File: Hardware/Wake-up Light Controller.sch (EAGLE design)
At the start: 46 parts, among them IC1 ST1S10, IC2 HT7333, IC3 DS3231/SO, IC4 ATMEGA328P_TQFP, J1 AVR-ISP, J2 Debug, Q1 BSS138, Q2 BSS138, Q3 FDN306P, Q4 IRLZ44N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

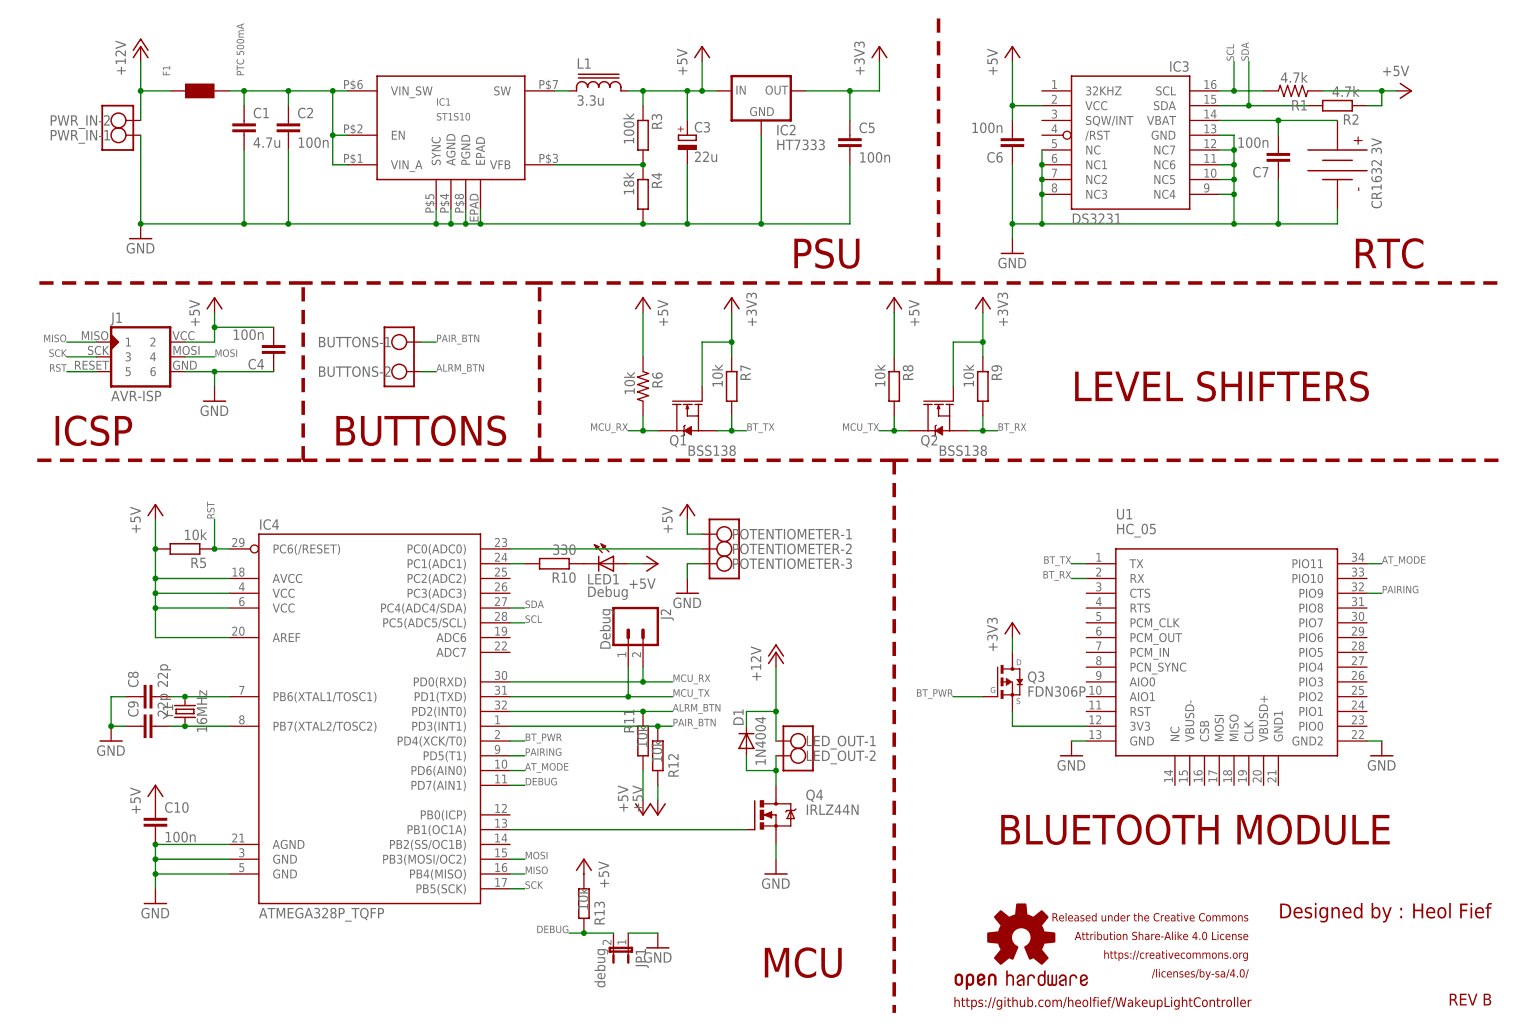
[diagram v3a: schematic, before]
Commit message: Add overvoltage protection
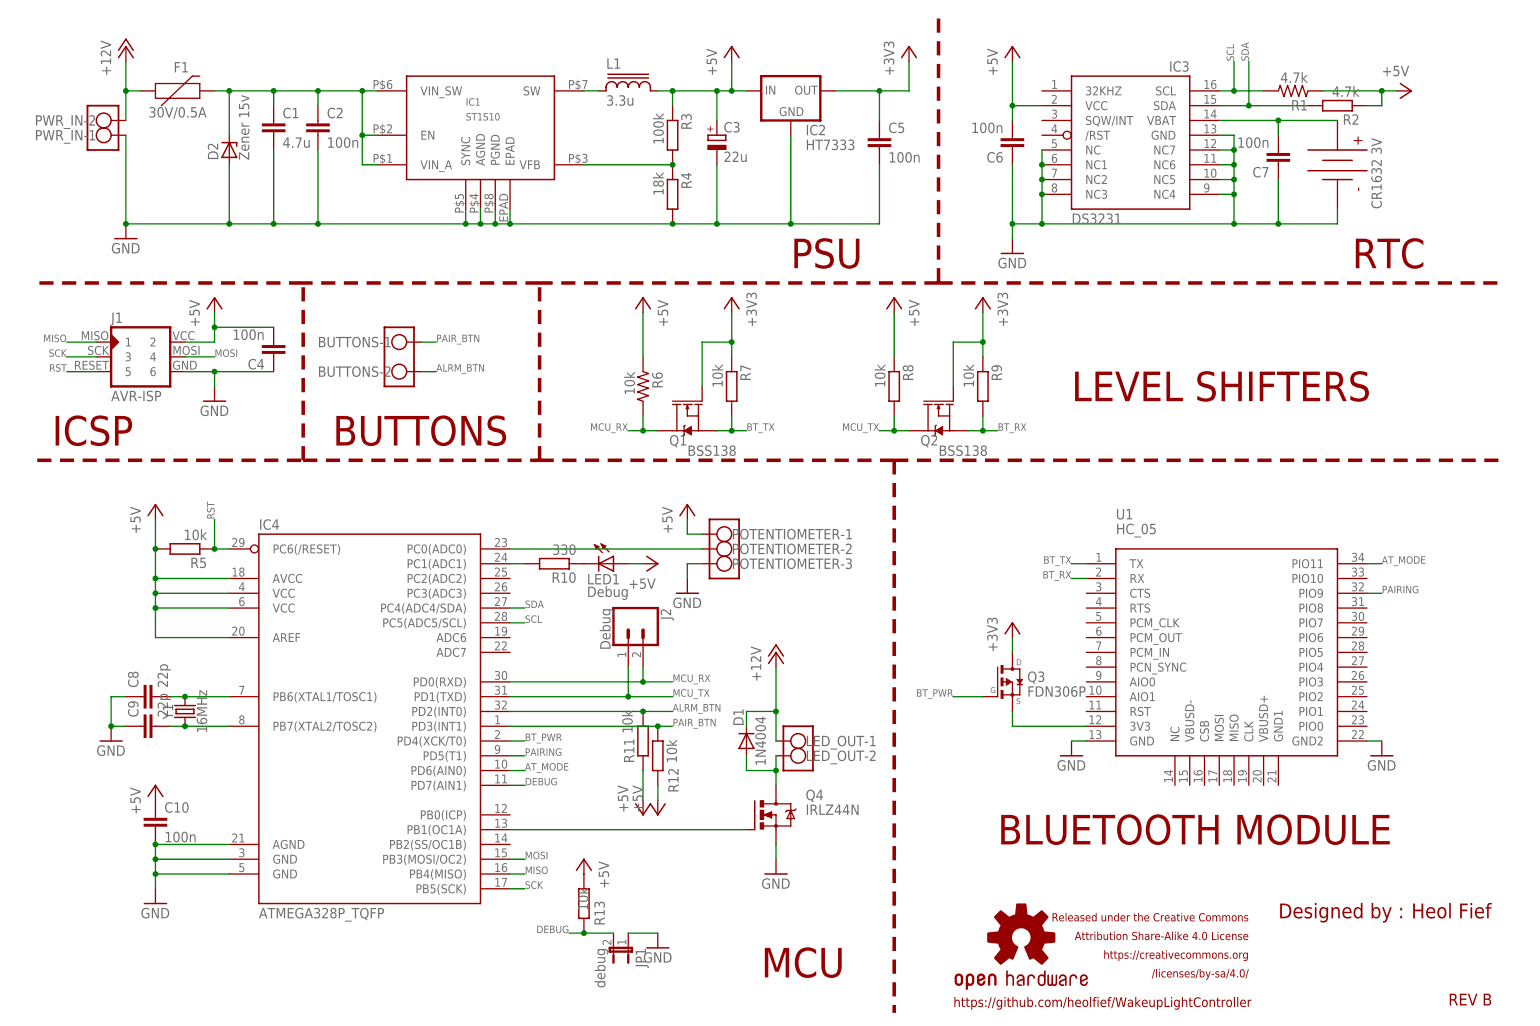
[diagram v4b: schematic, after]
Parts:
- added D2: Zener 15v, diode:ZENER-DIODESOD80C
- F1: value PTC 500mA -> 30V/0.5A; device BaseApp:PTC-0.2A-IH/0.5A-IT/40A-IM -> SparkFun-Fuses:PPTC_PTH
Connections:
- net GND: now also D2.A
- net N$9: now also D2.C
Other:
- moved on the sheet: C1, C2, C3, C5, IC1, IC2, L1, PWR_IN-1, PWR_IN-2, R3, R4

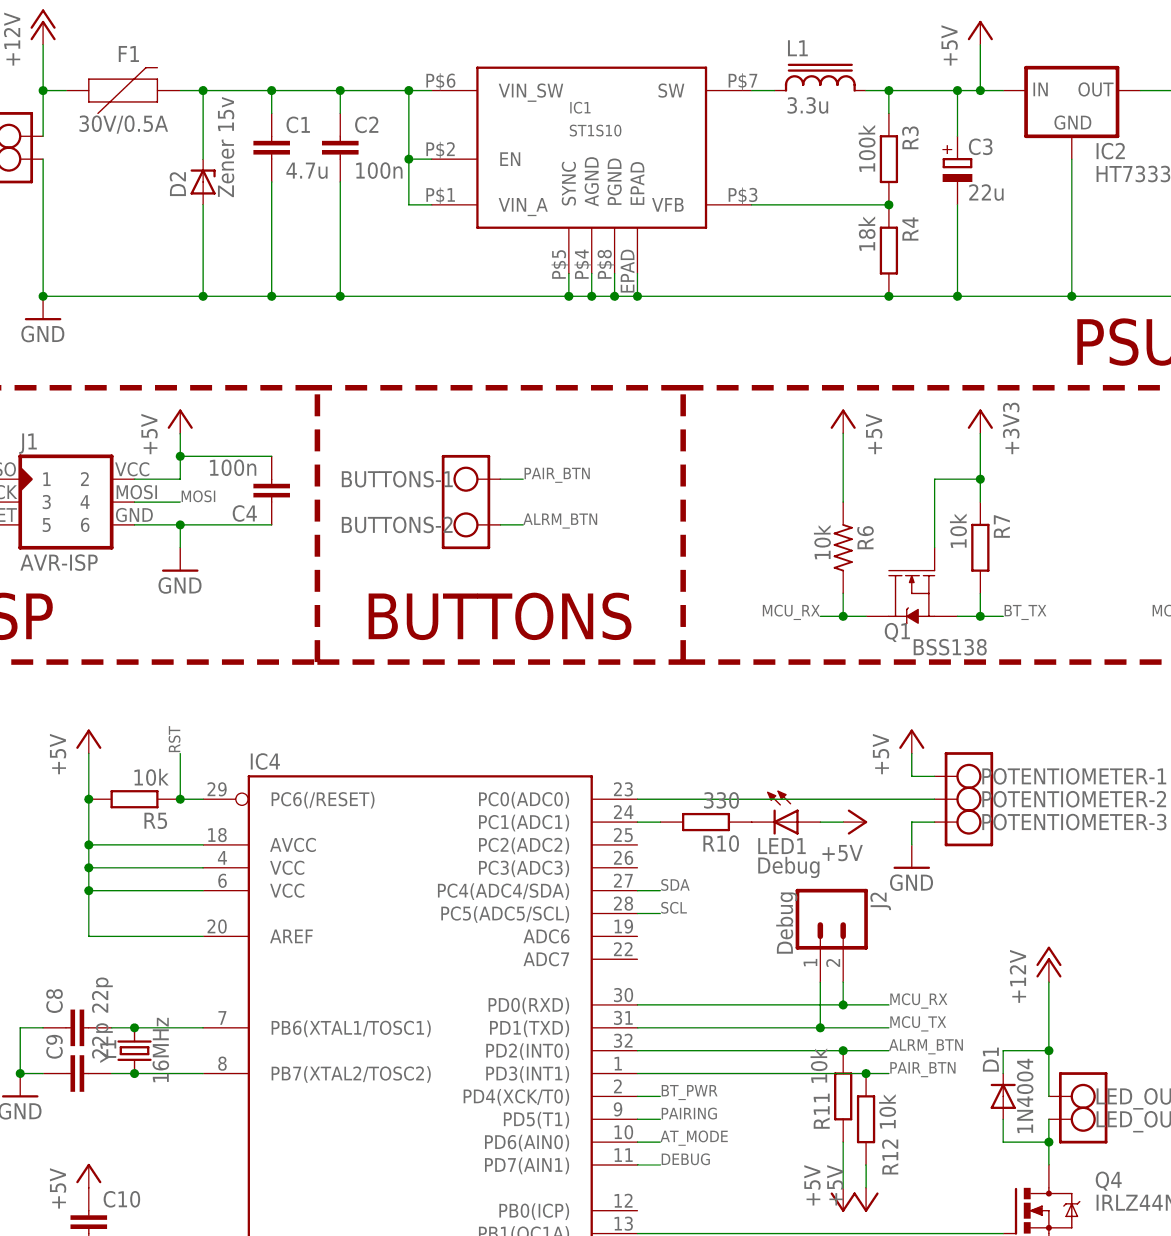
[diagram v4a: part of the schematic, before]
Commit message: Change diodes names
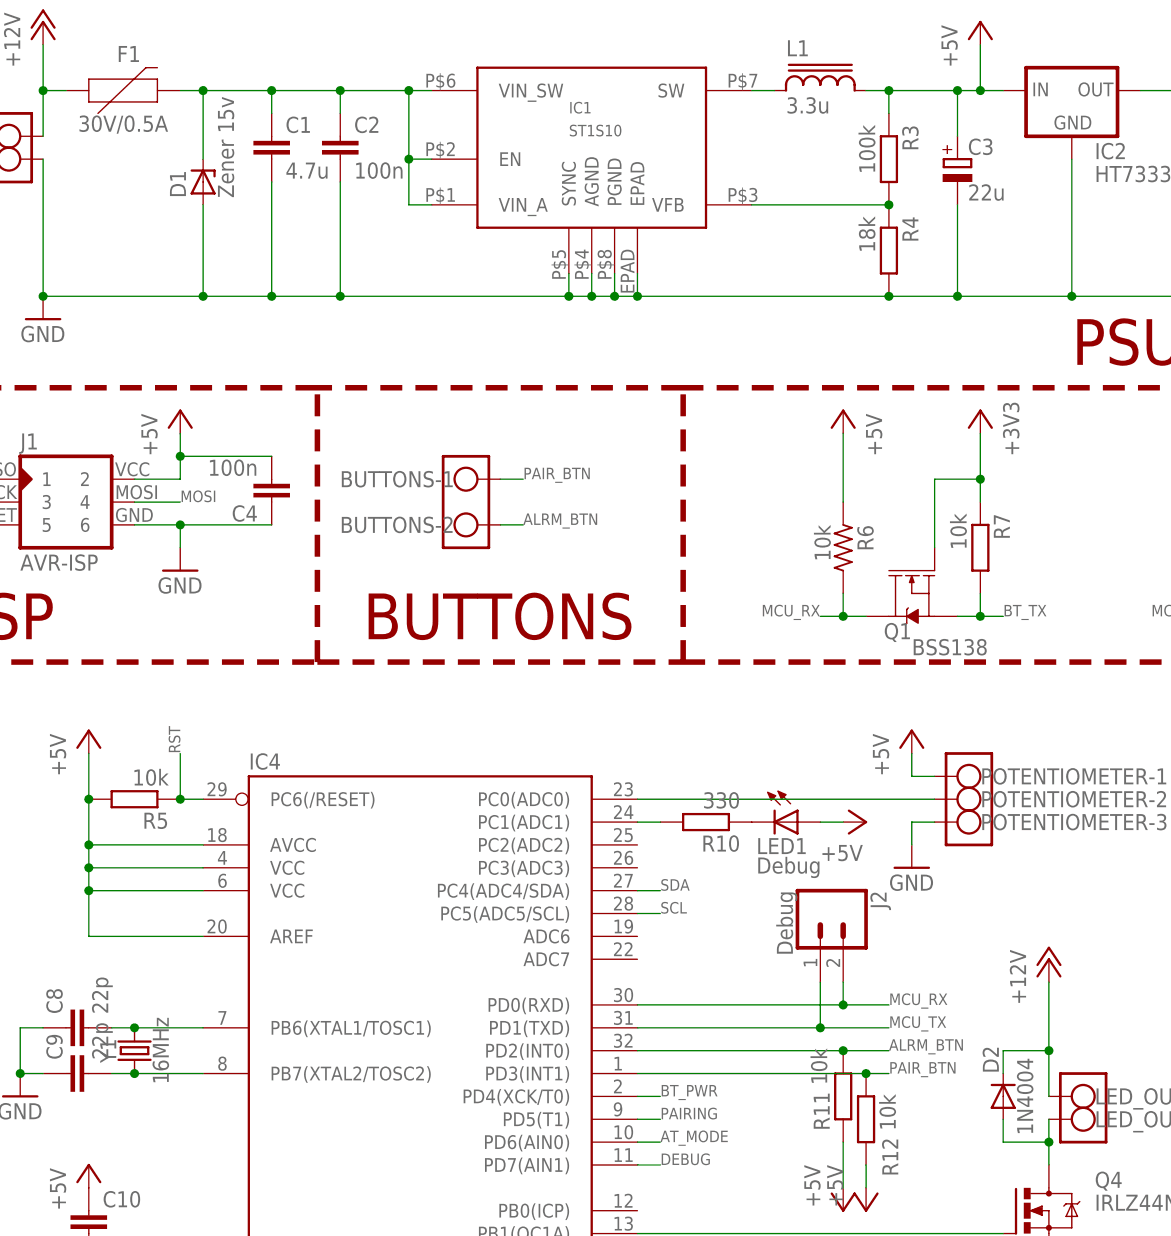
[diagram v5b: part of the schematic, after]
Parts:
- D1: value 1N4004 -> Zener 15v; device diode:DIODE-DO-214AC -> diode:ZENER-DIODESOD80C
- D2: value Zener 15v -> 1N4004; device diode:ZENER-DIODESOD80C -> diode:DIODE-DO-214AC
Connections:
- net +12V: now also D2.C; no longer D1.C
- net GND: now also D1.A; no longer D2.A
- net N$1: now also D2.A; no longer D1.A
- net N$9: now also D1.C; no longer D2.C
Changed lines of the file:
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@@
 <part name="P+8" library="supply1" deviceset="+12V" device=""/>
 <part name="GND8" library="supply1" deviceset="GND" device=""/>
-<part name="D1" library="diode" library_urn="urn:adsk.eagle:library:210" deviceset="DIODE-" device="DO-214AC" package3d_urn="urn:adsk.eagle:package:43416/2" value="1N4004"/>
+<part name="D2" library="diode" library_urn="urn:adsk.eagle:library:210" deviceset="DIODE-" device="DO-214AC" package3d_urn="urn:adsk.eagle:package:43416/2" value="1N4004"/>
 <part name="R5" library="resistor" library_urn="urn:adsk.eagle:library:348" deviceset="R-EU_" device="M0805" package3d_urn="urn:adsk.eagle:package:26079/1" value="10k"/>
 <part name="GND2" library="supply1" deviceset="GND" device=""/>
@@
 <part name="P+15" library="supply1" library_urn="urn:adsk.eagle:library:371" deviceset="+5V" device=""/>
 <part name="F1" library="SparkFun-Fuses" library_urn="urn:adsk.eagle:library:517" deviceset="PPTC" device="_PTH" package3d_urn="urn:adsk.eagle:package:38574/1" value="30V/0.5A"/>
-<part name="D2" library="diode" library_urn="urn:adsk.eagle:library:210" deviceset="ZENER-DIODE" device="SOD80C" package3d_urn="urn:adsk.eagle:package:43405/2" value="Zener 15v"/>
+<part name="D1" library="diode" library_urn="urn:adsk.eagle:library:210" deviceset="ZENER-DIODE" device="SOD80C" package3d_urn="urn:adsk.eagle:package:43405/2" value="Zener 15v"/>
 </parts>
 <sheets>
@@
 <instance part="P+8" gate="1" x="104.14" y="73.66"/>
 <instance part="GND8" gate="1" x="104.14" y="35.56"/>
-<instance part="D1" gate="G$1" x="99.06" y="58.42" smashed="yes" rot="R90">
+<instance part="D2" gate="G$1" x="99.06" y="58.42" smashed="yes" rot="R90">
 <attribute name="NAME" x="98.5774" y="60.96" size="1.778" layer="95" rot="R90"/>
 <attribute name="VALUE" x="102.3874" y="54.102" size="1.778" layer="96" rot="R90"/>
@@
 <instance part="P+15" gate="1" x="71.12" y="38.1" rot="MR0"/>
 <instance part="F1" gate="G$1" x="0" y="170.18"/>
-<instance part="D2" gate="G$1" x="10.16" y="160.02" rot="R90"/>
+<instance part="D1" gate="G$1" x="10.16" y="160.02" rot="R90"/>
 </instances>
 <busses>
@@
 <wire x1="-7.62" y1="162.56" x2="-7.62" y2="147.32" width="0.1524" layer="91"/>
 <junction x="-7.62" y="147.32"/>
-<pinref part="D2" gate="G$1" pin="A"/>
+<pinref part="D1" gate="G$1" pin="A"/>
 <wire x1="10.16" y1="157.48" x2="10.16" y2="147.32" width="0.1524" layer="91"/>
 <junction x="10.16" y="147.32"/>
@@
 <wire x1="104.14" y1="58.42" x2="104.14" y2="63.5" width="0.1524" layer="91"/>
 <pinref part="P+8" gate="1" pin="+12V"/>
-<pinref part="D1" gate="G$1" pin="C"/>
+<pinref part="D2" gate="G$1" pin="C"/>
 <wire x1="104.14" y1="63.5" x2="104.14" y2="71.12" width="0.1524" layer="91"/>
 <wire x1="99.06" y1="60.96" x2="99.06" y2="63.5" width="0.1524" layer="91"/>
@@
 <segment>
 <wire x1="104.14" y1="50.8" x2="104.14" y2="53.34" width="0.1524" layer="91"/>
-<pinref part="D1" gate="G$1" pin="A"/>
+<pinref part="D2" gate="G$1" pin="A"/>
 <wire x1="104.14" y1="53.34" x2="104.14" y2="55.88" width="0.1524" layer="91"/>
 <wire x1="99.06" y1="55.88" x2="99.06" y2="53.34" width="0.1524" layer="91"/>
@@
 <wire x1="7.62" y1="170.18" x2="10.16" y2="170.18" width="0.1524" layer="91"/>
 <junction x="17.78" y="170.18"/>
-<pinref part="D2" gate="G$1" pin="C"/>
+<pinref part="D1" gate="G$1" pin="C"/>
 <wire x1="10.16" y1="170.18" x2="17.78" y2="170.18" width="0.1524" layer="91"/>
 <wire x1="10.16" y1="162.56" x2="10.16" y2="170.18" width="0.1524" layer="91"/>

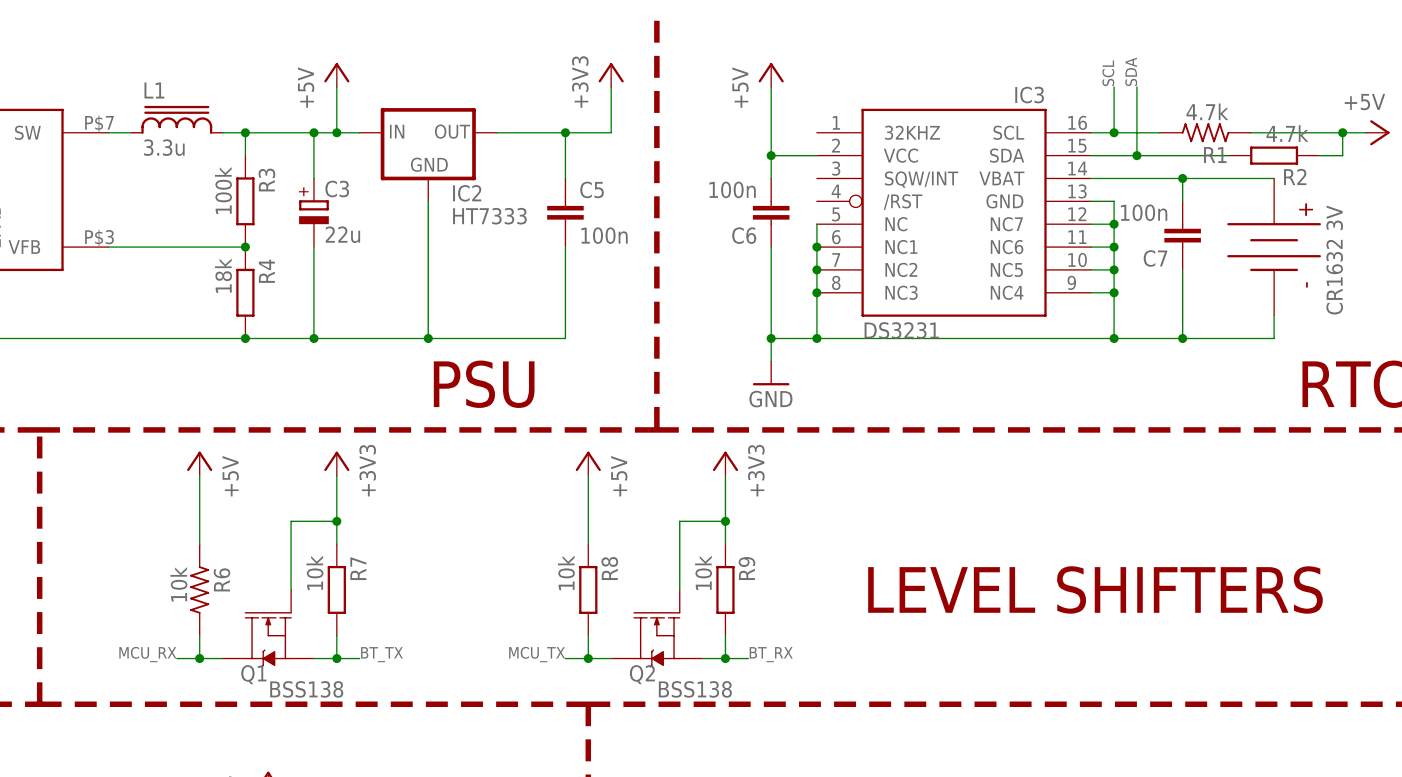
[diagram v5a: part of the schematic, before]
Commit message: Changed resistor pad spacing
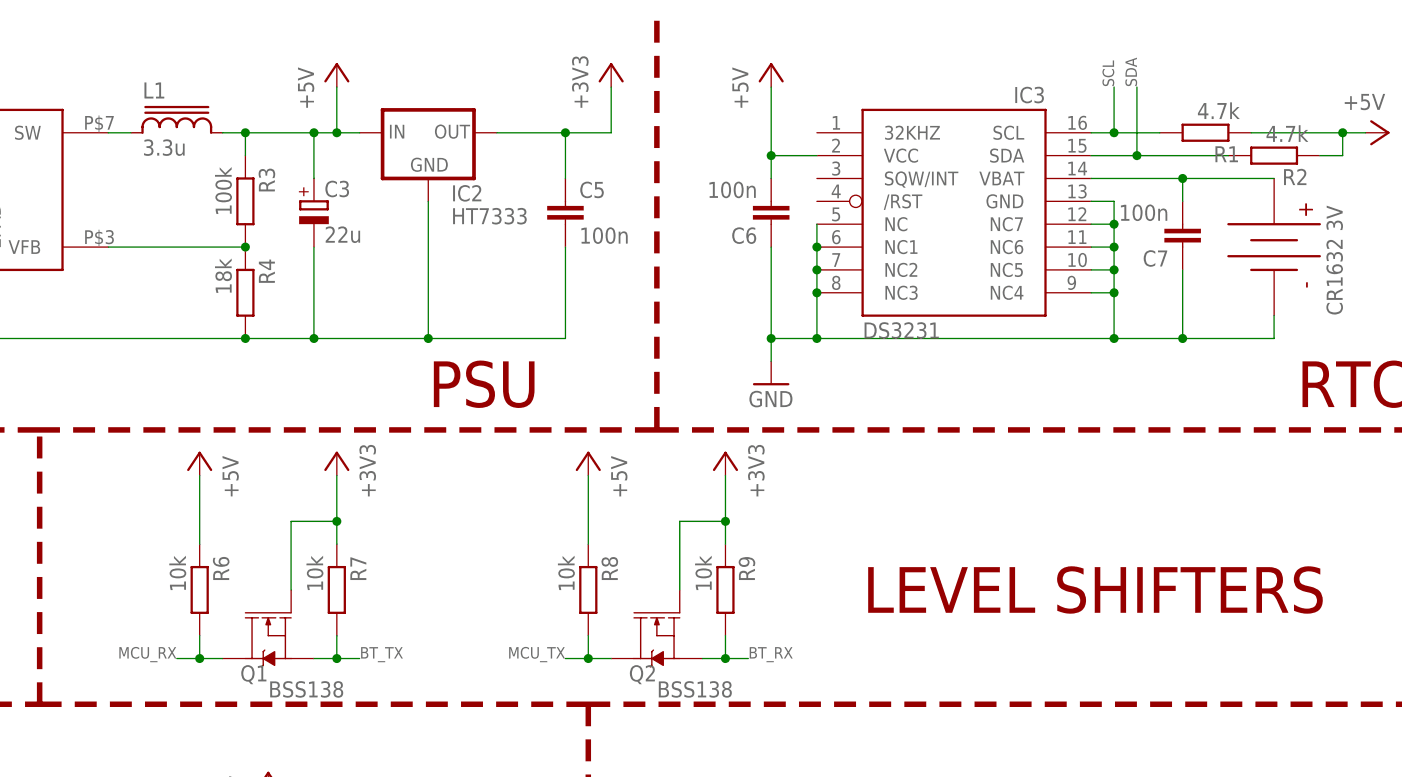
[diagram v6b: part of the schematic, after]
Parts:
- R1, R6: device rc-master-smd:R_0805MP -> heol:RESISTOR_EU
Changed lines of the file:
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@@
 <part name="C8" library="rcl" deviceset="C-EU" device="C0805" value="22p"/>
 <part name="GND5" library="supply1" deviceset="GND" device=""/>
-<part name="R1" library="rc-master-smd" deviceset="R_" device="0805MP" value="4.7k"/>
+<part name="R1" library="heol" deviceset="RESISTOR_EU" device="" value="4.7k"/>
 <part name="R2" library="resistor" library_urn="urn:adsk.eagle:library:348" deviceset="R-EU_" device="M0805" package3d_urn="urn:adsk.eagle:package:26079/1" value="4.7k"/>
 <part name="C7" library="rcl" deviceset="C-EU" device="C0805" value="100n"/>
@@
 <part name="+3V33" library="supply1" library_urn="urn:adsk.eagle:library:371" deviceset="+3V3" device=""/>
 <part name="+3V34" library="supply1" library_urn="urn:adsk.eagle:library:371" deviceset="+3V3" device=""/>
-<part name="R6" library="rc-master-smd" deviceset="R_" device="0805MP" value="10k"/>
+<part name="R6" library="heol" deviceset="RESISTOR_EU" device="" value="10k"/>
 <part name="R7" library="resistor" library_urn="urn:adsk.eagle:library:348" deviceset="R-EU_" device="M0805" package3d_urn="urn:adsk.eagle:package:26079/1" value="10k"/>
 <part name="R8" library="resistor" library_urn="urn:adsk.eagle:library:348" deviceset="R-EU_" device="M0805" package3d_urn="urn:adsk.eagle:package:26079/1" value="10k"/>
